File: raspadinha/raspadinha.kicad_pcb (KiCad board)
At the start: 2 copper layers, 143 x 79.5 mm, 0 parts

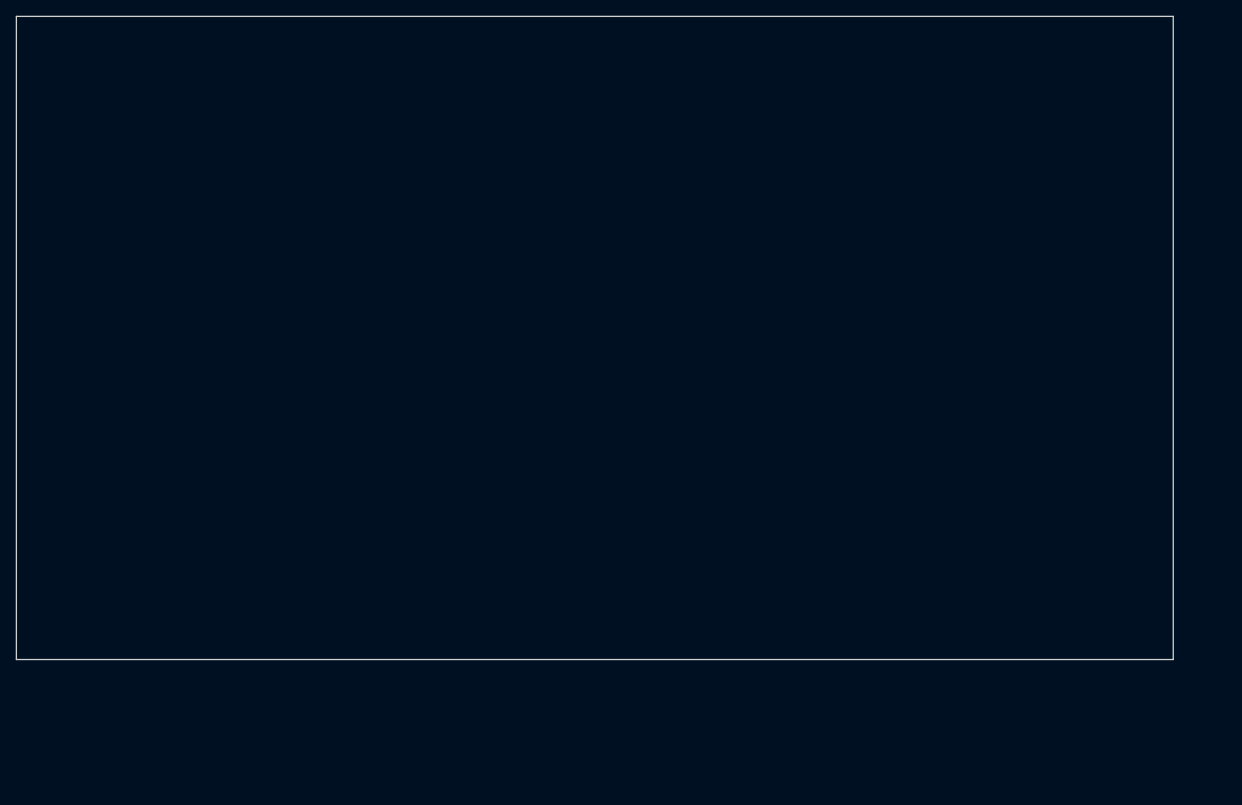
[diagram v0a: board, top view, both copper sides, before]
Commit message: feat: Posicionamento dos componentes na placa
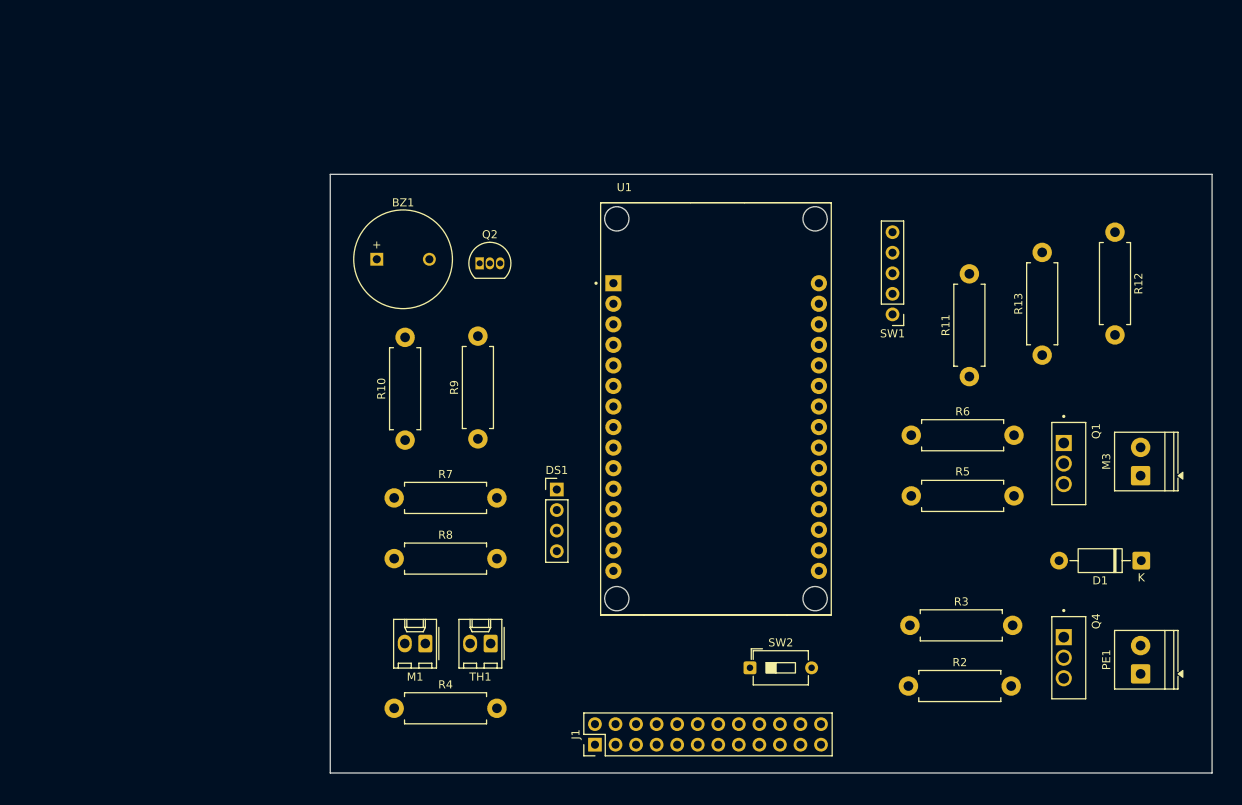
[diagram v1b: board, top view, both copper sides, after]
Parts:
- added BZ1: Buzzer, Buzzer_Beeper:MagneticBuzzer_ProSignal_ABT-410-RC, F.Cu at (106.5, 72.5)
- added D1: 1N4002, Diode_THT:D_DO-41_SOD81_P10.16mm_Horizontal, F.Cu at (201.0, 109.8)
- added DS1: ~, Connector_PinHeader_2.54mm:PinHeader_1x04_P2.54mm_Vertical, F.Cu at (128.8, 101.0)
- added J1: ATX-24, Connector_PinHeader_2.54mm:PinHeader_2x12_P2.54mm_Vertical, F.Cu at (133.5, 132.5)
- added M1: Fan, Connector_Molex:Molex_KK-254_AE-6410-02A_1x02_P2.54mm_Vertical, F.Cu at (112.5, 120.0)
- added M3: Motor_DC, TerminalBlock_Phoenix:TerminalBlock_Phoenix_PT-1,5-2-3.5-H_1x02_P3.50mm_Horizontal, F.Cu at (201.0, 99.3)
- added PE1: TEC1-12710, TerminalBlock_Phoenix:TerminalBlock_Phoenix_PT-1,5-2-3.5-H_1x02_P3.50mm_Horizontal, F.Cu at (201.0, 123.8)
- added Q1: IRFZ44N, IRFZ44N:TO254P1016X419X2286-3, F.Cu at (191.5, 97.8)
- added Q2: BC338, Package_TO_SOT_THT:TO-92_Inline, F.Cu at (119.3, 73.0)
- added Q4: IRFZ44N, IRFZ44N:TO254P1016X419X2286-3, F.Cu at (191.5, 121.8)
- added R10: 100R, Resistor_THT:R_Axial_DIN0411_L9.9mm_D3.6mm_P12.70mm_Horizontal, F.Cu at (110.0, 94.9)
- added R11: 10kR, Resistor_THT:R_Axial_DIN0411_L9.9mm_D3.6mm_P12.70mm_Horizontal, F.Cu at (179.8, 87.0)
- added R12: 10kR, Resistor_THT:R_Axial_DIN0411_L9.9mm_D3.6mm_P12.70mm_Horizontal, F.Cu at (197.8, 69.2)
- added R13: 10kR, Resistor_THT:R_Axial_DIN0411_L9.9mm_D3.6mm_P12.70mm_Horizontal, F.Cu at (188.8, 84.4)
- added R2: 10kR, Resistor_THT:R_Axial_DIN0411_L9.9mm_D3.6mm_P12.70mm_Horizontal, F.Cu at (172.3, 125.3)
- added R3: 100R, Resistor_THT:R_Axial_DIN0411_L9.9mm_D3.6mm_P12.70mm_Horizontal, F.Cu at (172.4, 117.8)
- added R4: 10kR, Resistor_THT:R_Axial_DIN0411_L9.9mm_D3.6mm_P12.70mm_Horizontal, F.Cu at (108.7, 128.0)
- added R5: 10kR, Resistor_THT:R_Axial_DIN0411_L9.9mm_D3.6mm_P12.70mm_Horizontal, F.Cu at (172.6, 101.8)
- added R6: 100R, Resistor_THT:R_Axial_DIN0411_L9.9mm_D3.6mm_P12.70mm_Horizontal, F.Cu at (172.6, 94.3)
- added R7: 10kR, Resistor_THT:R_Axial_DIN0411_L9.9mm_D3.6mm_P12.70mm_Horizontal, F.Cu at (108.7, 102.0)
- added R8: 10kR, Resistor_THT:R_Axial_DIN0411_L9.9mm_D3.6mm_P12.70mm_Horizontal, F.Cu at (108.7, 109.5)
- added R9: 10kR, Resistor_THT:R_Axial_DIN0411_L9.9mm_D3.6mm_P12.70mm_Horizontal, F.Cu at (119.0, 94.7)
- added SW1: RotaryEncoder_Switch, Connector_PinHeader_2.54mm:PinHeader_1x05_P2.54mm_Vertical, F.Cu at (170.3, 79.3)
- added SW2: SW_SPST, Button_Switch_THT:SW_DIP_SPSTx01_Slide_6.7x4.1mm_W7.62mm_P2.54mm_LowProfile, F.Cu at (152.7, 123.0)
- added TH1: NTC10K, Connector_Molex:Molex_KK-254_AE-6410-02A_1x02_P2.54mm_Vertical, F.Cu at (120.6, 120.0)
- added U1: ESP32-DEVKIT-V1, ESP32-DEVKIT-V1:MODULE_ESP32_DEVKIT_V1, F.Cu at (148.5, 91.0)
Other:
- board size 143 x 79.5 mm -> 109 x 74 mm

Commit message: feat: Refatoração da alimentação da placa feat: Renomeação do número dos componentes
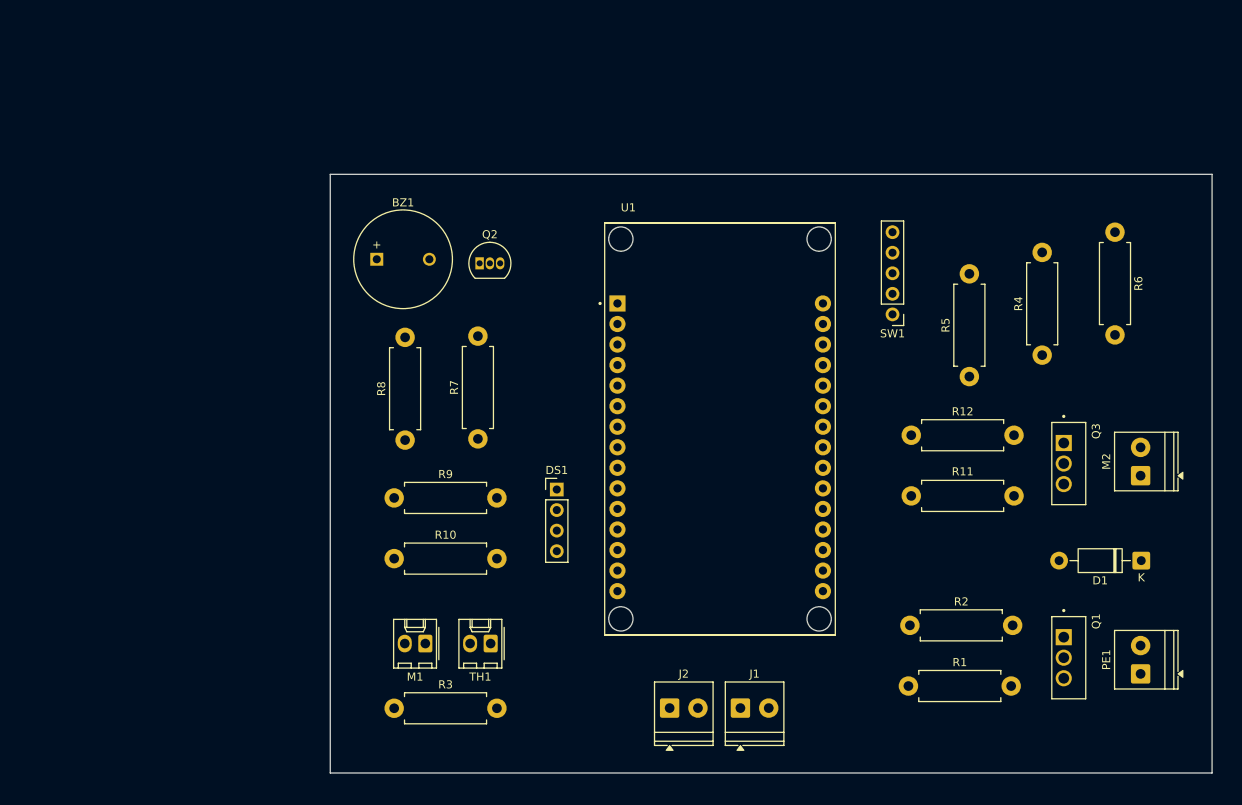
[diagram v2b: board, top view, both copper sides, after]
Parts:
- removed SW2: SW_SPST, Button_Switch_THT:SW_DIP_SPSTx01_Slide_6.7x4.1mm_W7.62mm_P2.54mm_LowProfile
- added J2: Screw_Terminal_01x02, TerminalBlock_Phoenix:TerminalBlock_Phoenix_PT-1,5-2-3.5-H_1x02_P3.50mm_Horizontal, F.Cu at (142.8, 128.0)
- J1: value ATX-24 -> Screw_Terminal_01x02; footprint Connector_PinHeader_2.54mm:PinHeader_2x12_P2.54mm_Vertical -> TerminalBlock_Phoenix:TerminalBlock_Phoenix_PT-1,5-2-3.5-H_1x02_P3.50mm_Horizontal
- moved J1 18.5 mm to (151.5, 128.0), turned to 0 degrees
- moved U1 2.55 mm to (149.0, 93.5)
- renumbered M3 to M2, Q4 to Q1, Q1 to Q3, R2 to R1, R8 to R10, R5 to R11, R6 to R12, R3 to R2, R4 to R3, R13 to R4, R11 to R5, R12 to R6, R9 to R7, R10 to R8, R7 to R9
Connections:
- J1 pad 1: +3.3V -> +5V
- J1 pad 2: +3.3V -> +12V

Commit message: feat: NetClasses
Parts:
- moved M1 8.08 mm to (120.6, 120.0)
- moved TH1 8.08 mm to (112.5, 120.0)
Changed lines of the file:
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@@
 	(footprint "Connector_Molex:Molex_KK-254_AE-6410-02A_1x02_P2.54mm_Vertical"
 		(layer "F.Cu")
-		(at 120.625 120.025 180)
+		(at 112.55 120.025 180)
 		(descr "Molex KK-254 Interconnect System, old/engineering part number: AE-6410-02A example for new part number: 22-27-2021, 2 Pins (http://www.molex.com/pdm_docs/sd/022272021_sd.pdf), generated with kicad-footprint-generator")
 		(tags "connector Molex KK-254 vertical")
@@
 	(footprint "Connector_Molex:Molex_KK-254_AE-6410-02A_1x02_P2.54mm_Vertical"
 		(layer "F.Cu")
-		(at 112.55 120.025 180)
+		(at 120.625 120.025 180)
 		(descr "Molex KK-254 Interconnect System, old/engineering part number: AE-6410-02A example for new part number: 22-27-2021, 2 Pins (http://www.molex.com/pdm_docs/sd/022272021_sd.pdf), generated with kicad-footprint-generator")
 		(tags "connector Molex KK-254 vertical")

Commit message: feat: Elementos roteados
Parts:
- moved D1 5.13 mm to (202.7, 104.9), turned to -90 degrees
- moved R1 2.97 mm to (169.3, 125.3)
- moved R11 2.97 mm to (169.7, 101.8)
- moved R12 2.97 mm to (169.7, 94.3)
- moved R2 2.97 mm to (169.5, 117.8)
- moved M2 1.70 mm to (202.7, 99.3)
- moved PE1 1.70 mm to (202.7, 123.8)
- moved Q1 0.97 mm to (190.5, 121.8), turned to 0 degrees
- moved Q3 0.97 mm to (190.5, 97.8), turned to 0 degrees
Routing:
- net +3.3V: track 0.00 -> 191.6 mm
- net +5V: track 0.00 -> 172.9 mm
- net +12V: track 0.00 -> 104.1 mm
- net TEMPERATURE_SIGNAL: track 0.00 -> 79.5 mm, vias 0 -> 2
- net ROTARY_SIGNAL_SWITCH: track 0.00 -> 52.6 mm
- net ROTARY_SIGNAL_B: track 0.00 -> 43.6 mm
- net ROTARY_SIGNAL_A: track 0.00 -> 34.6 mm
- net BUZZER_SIGNAL: track 0.00 -> 27.8 mm
- net PELTIER_SIGNAL: track 0.00 -> 27.7 mm
- net DISPLAY_SDA_SIGNAL: track 0.00 -> 25.6 mm
- net Net-(PE1-Pad1): track 0.00 -> 18.1 mm
- net MOTOR_SIGNAL: track 0.00 -> 17.1 mm
- net DISPLAY_SCL_SIGNAL: track 0.00 -> 16.3 mm
- net Net-(Q2-B): track 0.00 -> 15.1 mm
- net Net-(D1-K): track 0.00 -> 14.7 mm
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- added copper zone on B.Cu, net GND
